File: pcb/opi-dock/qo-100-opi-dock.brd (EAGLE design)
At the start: 75 x 60 mm, 149 parts, among them CON1 6P-SH-SIDE, CON10 3P-SH-TOP, CON11 3P-SH-TOP, CON12 3P-SH-TOP, CON13 3P-SH-TOP, CON14 3P-SH-SIDE, CON15 3P-SH-SIDE, CON16 3P-SH-SIDE, CON17 3P-SH-SIDE, CON18 2P-PH-TOP, CON19 2EDG-2P, CON2 6P-SH-SIDE, CON3 4P-SH-SIDE, CON4 4P-SH-SIDE, CON5 4P-SH-SIDE, CON6 4P-SH-SIDE, CON7 4P-SH-SIDE, CON8 3P-SH-TOP, CON9 3P-SH-TOP, Q1 AO3400, T1 BC817, T2 BC817, T3 BC817, T4 BC817, U1 ORANGEPIZERO, U10 CP2108, U12 DS2484, U13 LTC4313-1, U14 MCP1525, U15 MIC23155, U16 LT8640S, U17 MCP3221-A0, U2 MCP1703-330, U3 MCP23008, U4 LTC4313-2, U5 ADUM1250, U6 MCP1703-330, U7 MCP23008, U8 LTC4313-2, U9 ADUM1250

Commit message: Work on OPi dock
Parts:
- removed D1, D2, D3, D4: B0530W, Generic Diode:SOD-123
- removed R32, R33, R34, R35: 1K Ohms, Resistor:RES0603
- removed R43, R44, R45, R46: DNP, Resistor:RES0603
- removed T1, T2, T3, T4: BC817, Generic BJT:SOT23
- CON19: value 2EDG-2P -> 2EDG-2P-5MM; device Generic Connector:2EDG-2P -> Generic Connector:2EDG-2P-5MM
- LOGO1: value JS-5MM -> JS-10MM; device Silkscreen:JS_5MM -> Silkscreen:JS_10MM
- R24, R25, R30, R31: value 10K Ohms -> 100 Ohms
- R26, R27, R28, R29: value 1K Ohms -> 100 Ohms
- moved LOGO1 34.3 mm to (25.6, 47.0), turned to 90 degrees
- moved R24 31.9 mm to (11.4, 51.3), turned to 270 degrees
- moved R25 28.3 mm to (9.60, 51.3), turned to 270 degrees
- moved D8 23.2 mm to (7.80, 51.3), turned to 270 degrees
- moved R26 22.6 mm to (18.4, 51.3), turned to 270 degrees
- moved R39 22.5 mm to (8.70, 48.8)
- moved R28 21.9 mm to (25.4, 51.3), turned to 270 degrees
- moved CON14 21.0 mm to (10.0, 58.0)
- moved CON17 21.0 mm to (31.0, 58.0)
- moved R36 20.0 mm to (29.7, 48.8)
- moved R27 19.9 mm to (16.6, 51.3), turned to 270 degrees
- moved D5 18.8 mm to (28.8, 51.3), turned to 270 degrees
- moved R29 16.9 mm to (23.6, 51.3), turned to 270 degrees
- moved R31 11.2 mm to (30.6, 51.3), turned to 270 degrees
- moved R30 9.53 mm to (32.4, 51.3), turned to 270 degrees
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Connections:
- removed net N$26: R24.1, T1.1
- removed net N$27: R25.1, T2.1
- removed net N$28: R30.1, T3.1
- removed net N$29: R31.1, T4.1
- removed net N$30: CON14.1, R43.1
- removed net N$31: CON17.1, R46.1
- removed net N$32: CON16.1, R45.1
- removed net N$33: CON15.1, R44.1
- removed net UART0_TRX: CON14.2, D1.A, R28.1, T1.2
- removed net UART1_TRX: CON15.2, D2.A, R29.1, T2.2
- removed net UART2_TRX: CON16.2, D3.A, R34.1, T3.2
- removed net UART3_TRX: CON17.2, D4.A, R35.1, T4.2
- new net N$12: CON14.2, R25.1
- new net N$14: CON14.1, R24.1
- new net N$16: CON15.2, R27.1
- new net N$17: CON15.1, R26.1
- new net N$20: CON16.2, R29.1
- new net N$21: CON16.1, R28.1
- new net N$23: CON17.2, R31.1
- new net N$24: CON17.1, R30.1
- net 3V3: no longer R26.2, R27.2, R28.2, R29.2, R32.2, R33.2, R34.2, R35.2, R43.2, R44.2, R45.2, R46.2
- net GND: now also U1.GND@0, U1.GND@1, U1.GND@2, U1.GND@3
- net UART0_RX: now also R25.2; no longer R26.1, T1.3
- net UART0_TX: no longer D1.C
- net UART1_RX: now also R27.2; no longer R27.1, T2.3
- net UART1_TX: now also R26.2; no longer D2.C, R25.2
- net UART2_RX: now also R29.2; no longer R32.1, T3.3
- net UART2_TX: now also R28.2; no longer D3.C, R30.2
- net UART3_RX: now also R31.2; no longer R33.1, T4.3
- net UART3_TX: now also R30.2; no longer D4.C, R31.2
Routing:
- net 3V3: track 391.8 -> 338.1 mm
- net UART0_RX: track 62.5 -> 19.7 mm, vias 4 -> 2
- net UART0_TX: track 63.5 -> 21.7 mm, vias 4 -> 2
- net UART0_TRX: track 38.4 -> 0.00 mm, vias 3 -> 0
- net UART1_TRX: track 36.0 -> 0.00 mm, vias 4 -> 0
- net UART3_TRX: track 34.4 -> 0.00 mm, vias 4 -> 0
- net UART2_TRX: track 32.9 -> 0.00 mm, vias 4 -> 0
- net UART1_TX: track 39.0 -> 18.9 mm, vias 4 -> 2
- net UART1_RX: track 35.1 -> 16.9 mm, vias 4 -> 2
- net !UART0_ACTIVE: track 30.6 -> 14.0 mm
- net UART3_TX: track 24.2 -> 36.0 mm
- net UART3_RX: track 27.8 -> 38.7 mm
- net !UART3_ACTIVE: track 22.4 -> 31.2 mm
- net N$19: track 5.22 -> 9.80 mm
- net 5V0_SS: track 6.64 -> 2.73 mm
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
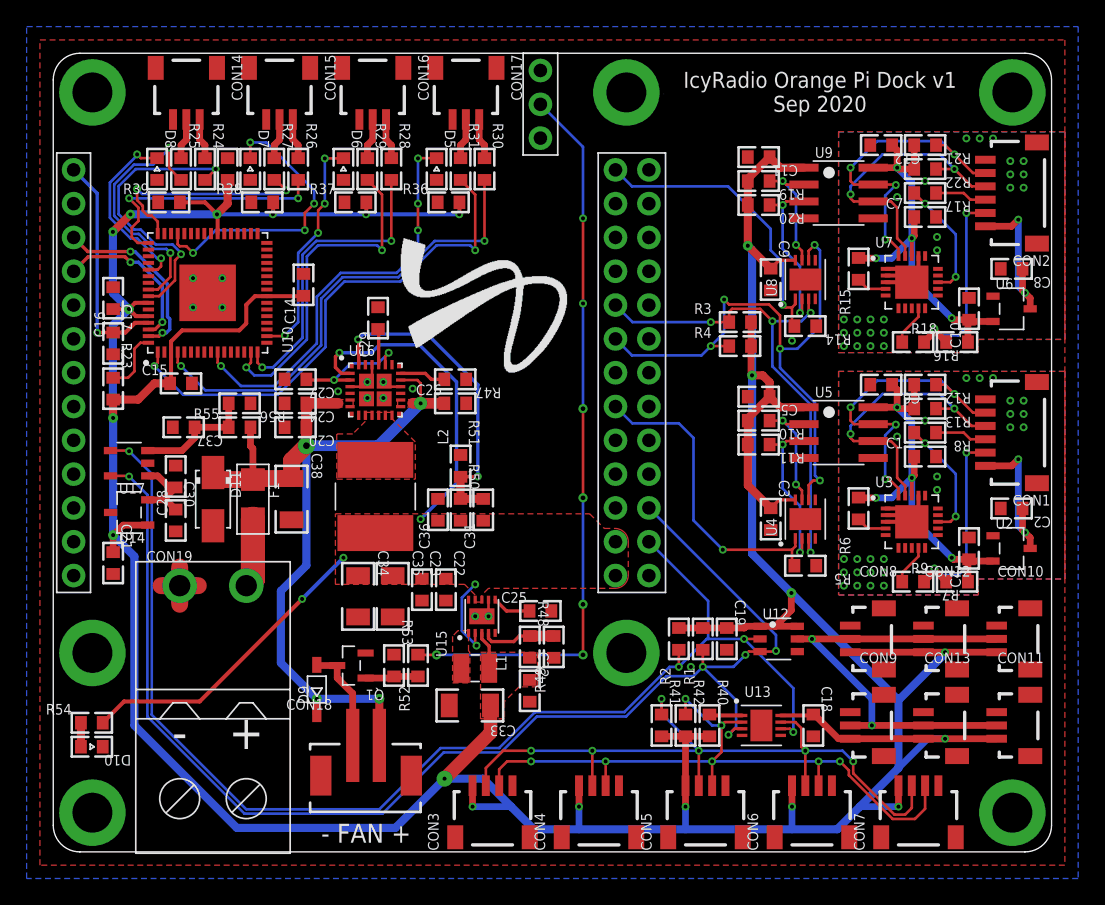
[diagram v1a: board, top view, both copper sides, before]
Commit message: Work on OPi dock Added connector for reed switches for intrusion detection
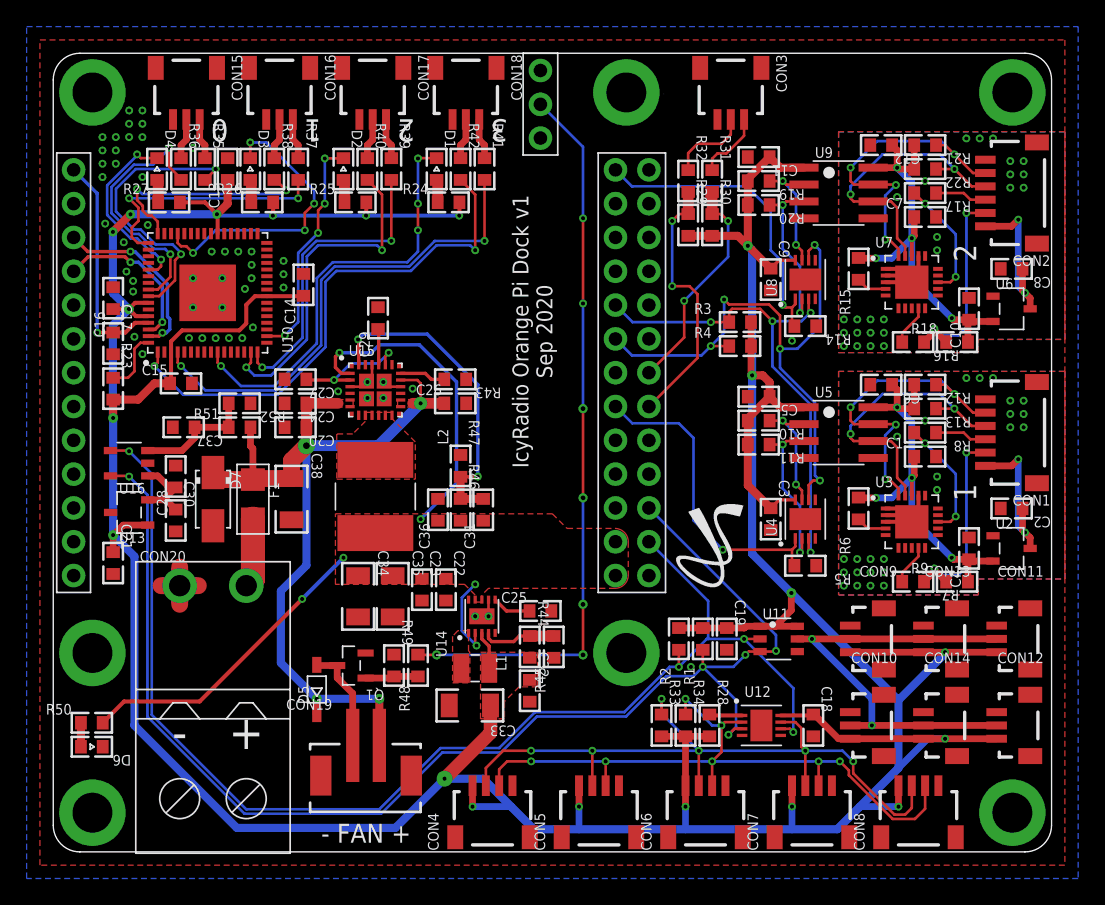
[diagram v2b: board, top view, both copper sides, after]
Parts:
- removed D10: LED0603, LED:0603
- removed D11: SMAJ12A, TVS:DO214AC
- removed D9: B0530W, Generic Diode:SOD-123
- removed R53: 10K Ohms, Resistor:RES0603
- removed R54: 510 Ohms, Resistor:RES0603
- removed R55: 147K Ohms, Resistor:RES0603
- removed R56: 21K Ohms, Resistor:RES0603
- removed U17: MCP3221-A0, Microchip:SOT23-5
- added CON20: 2EDG-2P-5MM, Generic Connector:2EDG-2P-5MM
- added D1, D2, D3: LED0603, LED:0603
- added R32, R35: 100 Ohms, Resistor:RES0603
- added R33, R34: 1K Ohms, Resistor:RES0603
- added R43: 41.2K Ohms, Resistor:RES0603
- added R44: 309K Ohms, Resistor:RES0603
- added R45: 71.5K Ohms, Resistor:RES0603
- added R46: 1M Ohms, Resistor:RES0603
- added U11: DS2484, Maxim Integrated:SOT23-6
- CON14: value 3P-SH-SIDE -> 3P-SH-TOP; device JST:SH-03-SIDE -> JST:SH-03-TOP
- CON18: value 2P-PH-TOP -> 3P-SH-SIDE; device JST:PH-02-TOP -> JST:SH-03-SIDE
- CON19: value 2EDG-2P-5MM -> 2P-PH-TOP; device Generic Connector:2EDG-2P-5MM -> JST:PH-02-TOP
- CON3: value 4P-SH-SIDE -> 3P-SH-SIDE; device JST:SH-04-SIDE -> JST:SH-03-SIDE
- CON8: value 3P-SH-TOP -> 4P-SH-SIDE; device JST:SH-03-TOP -> JST:SH-04-SIDE
- D5: value LED0603 -> B0530W; device LED:0603 -> Generic Diode:SOD-123
- D7: value LED0603 -> SMAJ12A; device LED:0603 -> TVS:DO214AC
- LOGO1: value JS-10MM -> JS-5MM; device Silkscreen:JS_10MM -> Silkscreen:JS_5MM
- R24, R25, R26, R27: value 100 Ohms -> 330 Ohms
- R28, R29, R30: value 100 Ohms -> 10K Ohms
- R36, R37, R38, R39: value 330 Ohms -> 100 Ohms
- R40: value 10K Ohms -> 100 Ohms
- R41, R42: value 1K Ohms -> 100 Ohms
- R47: value 41.2K Ohms -> 226K Ohms
- R48: value 309K Ohms -> 22 Ohms
- R49: value 71.5K Ohms -> 10K Ohms
- R50: value 1M Ohms -> 510 Ohms
- R51: value 226K Ohms -> 147K Ohms
- R52: value 22 Ohms -> 21K Ohms
- U12: value DS2484 -> LTC4313-1; device Maxim Integrated:SOT23-6 -> Analog Devices:DFN8
- U13: value LTC4313-1 -> MCP1525; device Analog Devices:DFN8 -> Microchip:SOT23
- U14: value MCP1525 -> MIC23155; device Microchip:SOT23 -> Microchip:DFN10
- U15: value MIC23155 -> LT8640S; device Microchip:DFN10 -> Analog Devices:QFN24_CORNER
- U16: value LT8640S -> MCP3221-A0; device Analog Devices:QFN24_CORNER -> Microchip:SOT23-5
- U2, U6: value MCP1703-330 -> MCP1703-500
- moved CON14 74.8 mm to (67.0, 9.50), turned to 270 degrees
- moved CON3 58.8 mm to (50.9, 58.0), turned to 180 degrees
- moved CON18 52.5 mm to (31.0, 58.0)
- moved U13 50.1 mm to (5.70, 25.5), turned to 180 degrees
- moved R40 49.1 mm to (23.6, 51.3)
- moved R28 48.2 mm to (49.3, 9.50)
- moved D6 47.3 mm to (2.90, 7.90), turned to 180 degrees
- moved R42 45.1 mm to (30.6, 51.3)
- moved R41 43.9 mm to (32.4, 51.3)
- moved D5 40.1 mm to (19.8, 12.2), turned to 90 degrees
- moved LOGO1 33.6 mm to (52.0, 26.3), turned to 0 degrees
- moved R50 32.0 mm to (2.90, 9.70), turned to 0 degrees
- moved U14 27.6 mm to (32.2, 17.7), turned to 90 degrees
- moved D7 25.0 mm to (12.0, 26.5)
- moved R29 24.5 mm to (47.7, 47.1)
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- renumbered D8 to D4
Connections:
- net 3V3SB_PSU1 renamed 5V0SB_PSU1
- net 3V3SB_PSU2 renamed 5V0SB_PSU2
- new net LOWER_OPEN: R29.1, R32.2, U1.MH$11
- new net N$26: CON3.2, R32.1
- new net N$27: CON3.1, R31.1
- new net UPPER_OPEN: R30.1, R31.2, U1.MH$13
- net !UART1_ACTIVE: now also D3.C; no longer D7.C
- net !UART2_ACTIVE: now also D2.C; no longer D6.C
- net !UART3_ACTIVE: now also D1.C; no longer D5.C
- net 2V5_ADC_CLEAN: now also U13.2, U16.1; no longer U14.2, U17.1
- net 3V3: now also CON14.1, R24.2, R25.2, R26.2, R27.2, R28.2, R29.2, R30.2, R33.2, R34.2, R44.2, U11.1, U11.6, U12.8, U13.1, U14.3; no longer CON3.1, R36.2, R37.2, R38.2, R39.2, R40.2, R41.2, R42.2, R48.2, U12.1, U12.6, U13.8, U14.1, U15.3
- net 3V3_FB: now also R44.1, R45.2, U14.4; no longer R48.1, R49.2, U15.4
- net 3V3_SOFTSTART: now also U14.6; no longer U15.6
- net 3V3_SW: now also U14.1; no longer U15.1
- net 5V0: now also R46.2, U14.2, U14.8, U14.9, U15.1; no longer R54.2, U15.2, U15.8, U15.9, U16.1
- net 5V0_FB: now also R46.1, R47.2, U15.24; no longer R50.1, R51.2, U16.24
- net 5V0_INTVCC: now also U15.2, U15.20; no longer U16.2, U16.20
- net 5V0_RT: now also R43.2, U15.18; no longer R47.2, U16.18
- net 5V0_SS: now also U15.21; no longer U16.21
- net 5V0_SW: now also U15.10, U15.11, U15.12, U15.8, U15.9; no longer U16.10, U16.11, U16.12, U16.8, U16.9
- net FAN_PWM: now also R48.2; no longer R52.2
- net GND: now also CON18.3, CON20.P$1, CON3.3, CON8.4, D6.C, D7.A, R43.1, R45.1, R52.1, U11.4, U12.9, U13.3, U14.10, U14.11, U14.7, U15.16, U15.22, U15.25, U15.26, U15.27, U15.28, U15.29, U15.3, U15.30, U15.31, U15.32, U16.2; no longer CON19.P$1, CON3.4, CON8.3, D10.C, D11.A, R51.1, R53.1, R56.1, U13.4, U13.9, U14.3, U15.10, U15.11, U15.7, U16.16, U16.22, U16.25, U16.26, U16.27, U16.28, U16.29, U16.3, U16.30, U16.31, U16.32, U17.2
- net I2C0_SCL: now also U11.3, U16.5; no longer U13.3, U17.5
- net I2C0_SDA: now also U11.2, U12.6, U16.4; no longer U12.2, U13.6, U17.4
- net I2C_SCL_EXT: now also CON8.3, R34.1, U12.2; no longer CON3.3, R42.1, U13.2
- net I2C_SDA_EXT: now also CON8.2, R33.1, U12.7; no longer CON3.2, R41.1, U13.7
- net N$12: now also CON15.2, R36.1; no longer CON14.2, R25.1
- net N$13: now also R28.1, U12.1; no longer R40.1, U13.1
- net N$14: now also CON15.1, R35.1; no longer CON14.1, R24.1
- net N$149: now also D6.A, R50.1; no longer D10.A, R54.1
- net N$15: now also R27.1; no longer R39.1
- net N$16: now also CON16.2, R38.1; no longer CON15.2, R27.1
- net N$17: now also CON16.1, R37.1; no longer CON15.1, R26.1
- net N$18: now also D3.A, R26.1; no longer D7.A, R38.1
- net N$19: now also CON20.P$2; no longer CON19.P$2
- net N$20: now also CON17.2, R40.1; no longer CON16.2, R29.1
- net N$21: now also CON17.1, R39.1; no longer CON16.1, R28.1
- net N$22: now also D2.A, R25.1; no longer D6.A, R37.1
- net N$23: now also CON18.2, R42.1; no longer CON17.2, R31.1
- net N$24: now also CON18.1, R41.1; no longer CON17.1, R30.1
- net N$25: now also D1.A, R24.1; no longer D5.A, R36.1
- net N$34: now also CON19.2, D5.A; no longer CON18.2, D9.A
- net N$35: now also R48.1, R49.2; no longer R52.1, R53.2
- net OW_BUS: now also CON14.2, U11.5; no longer CON8.2, U12.5
- net UART0_RX: now also R36.2; no longer R25.2
- net UART0_TX: now also R35.2; no longer R24.2
- net UART1_RX: now also R38.2; no longer R27.2
- net UART1_TX: now also R37.2; no longer R26.2
- net UART2_RX: now also R40.2; no longer R29.2
- net UART2_TX: now also R39.2; no longer R28.2
- net UART3_RX: now also R42.2; no longer R31.2
- net UART3_TX: now also R41.2; no longer R30.2
- net VIN: now also CON19.1, D5.C, D7.C, R51.2, U15.13, U15.14, U15.17, U15.5, U15.6; no longer CON18.1, D11.C, D9.C, R55.2, U16.13, U16.14, U16.17, U16.5, U16.6
- net VIN_VSENSE: now also R51.1, R52.2, U16.3; no longer R55.1, R56.2, U17.3
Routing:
- net LOWER_OPEN: track 0.00 -> 20.1 mm, vias 0 -> 2
- net UPPER_OPEN: track 0.00 -> 16.9 mm, vias 0 -> 2
- net N$26: track 0.00 -> 6.19 mm
- net N$27: track 0.00 -> 5.19 mm
- net 3V3: track 338.1 -> 343.2 mm
- net N$18: track 0.00 -> 1.71 mm
- net N$15: track 0.00 -> 1.71 mm
- net N$25: track 0.00 -> 1.71 mm
- net N$22: track 0.00 -> 1.71 mm
- net UART3_TX: track 36.0 -> 36.8 mm
- net UART3_RX: track 38.7 -> 39.6 mm
- net PSU2_I2C_EN: track 22.6 -> 23.4 mm
- net !UART3_ACTIVE: track 31.2 -> 32.0 mm
- net GND: vias 17 -> 56
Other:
- board text added: "0"
- board text added: "1"
- board text added: "2"
- board text added: "3"
